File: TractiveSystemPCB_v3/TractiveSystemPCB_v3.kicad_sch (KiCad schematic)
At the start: 42 parts, among them J1 TS, Q1 2N7002, Q4 RSC002, Q7 2N7002, U1 LM311, U6 4N35, U7 NE555D

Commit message: Update KiCADReferencingInstructions.docx, TractiveSystemPCB_v3-2022-09-27_114516.zip, and 9 more files...
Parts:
- added C2: 10nF, symbol GRC_Device:C_Small
- added D?: 17VBD, symbol GRC_Device:D_Zener
- added F?: Fuse_Small, symbol GRC_Device:Fuse_Small
- added R19: 20kΩ, symbol GRC_Device:R_Small
- added R20: 1.2kΩ, symbol GRC_Device:R_Small
- added R22: 10kΩ, symbol GRC_Device:R_Small
- added R?: 0Ω, symbol GRC_Device:R_Small
- added TP4: TestPoint, symbol GRC_Connector:TestPoint
- added U5: 4N35, Package_DIP:DIP-6_W7.62mm, symbol GRC_Isolator:4N35
- gave numbers to parts that had none: 3
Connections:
- net +12V: now also U3.8 (V+), R19.2, U5.1
- net +GLV: now also U5.5
- net BusRefPrecharge: now also F?.1, R?.1
- net GLV-: now also R22.2
- net GND: now also U3.1 (GND), U3.4 (V-), D?.2 (A)
- net PrechargeRef: now reaches RV2.2, TP3.1
- net PrechargeRef: now also U3.3 (-), C2.2
- net at U3.2 (+): now also C2.1, D?.1 (K), F?.2, R?.2, TP4.1
- net at U3.5 (BAL): now also U3.6 (STRB)
- net at U3.7: now also R19.1, R20.2
- new net: R20.1, U5.2
- new net: R22.1, U5.4
- no-connect marks 1 -> 2
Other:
- note added: "Precharge Control"
- note added: "Precharge Reference"
- note added: "TSAL Reference"
- moved on the sheet: RV1, RV2, TP2, TP3, U3

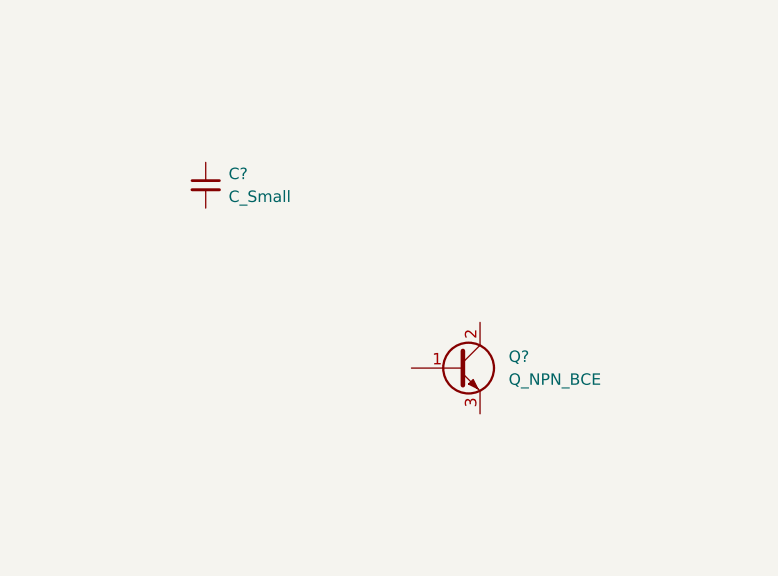
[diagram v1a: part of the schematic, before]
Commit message: Update BSPD 2.0-2022-11-05_114535.zip, Connector_Generic.kicad_sym, and 16 more files...
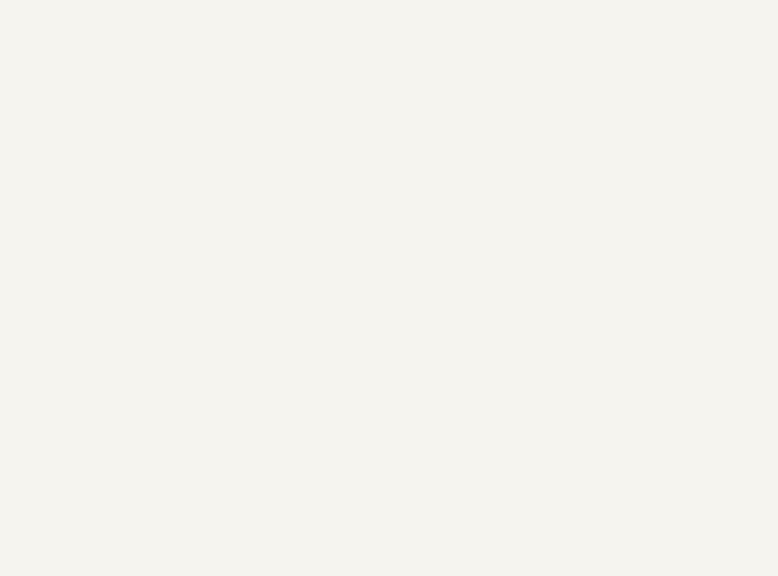
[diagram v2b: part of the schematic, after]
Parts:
- removed C?: C_Small, symbol GRC_Device:C_Small
- removed Q?: Q_NPN_BCE, symbol GRC_Device:Q_NPN_BCE
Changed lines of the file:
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@@
     (pin "1")
-  )
-  (symbol (lib_id "GRC_Device:C_Small") (at 223.52 118.11 0) (unit 1)
-    (in_bom yes) (on_board yes) (fields_autoplaced)
-    (property "Reference" "C?" (id 0) (at 226.06 116.8462 0)
-      (effects (font (size 1.27 1.27)) (justify left))
-    )
-    (property "Value" "C_Small" (id 1) (at 226.06 119.3862 0)
-      (effects (font (size 1.27 1.27)) (justify left))
-    )
-    (property "Footprint" "" (id 2) (at 223.52 118.11 0)
-      (effects (font (size 1.27 1.27)) hide)
-    )
-    (property "Datasheet" "~" (id 3) (at 223.52 118.11 0)
-      (effects (font (size 1.27 1.27)) hide)
-    )
-    (pin "1")
-    (pin "2")
   )
   (symbol (lib_id "GRC_glv-:GLV-") (at 140.335 120.015 0) (unit 1)
@@
     (pin "1")
   )
-  (symbol (lib_id "GRC_Device:Q_NPN_BCE") (at 251.46 138.43 0) (unit 1)
-    (in_bom yes) (on_board yes) (fields_autoplaced)
-    (property "Reference" "Q?" (id 0) (at 257.175 137.1599 0)
-      (effects (font (size 1.27 1.27)) (justify left))
-    )
-    (property "Value" "Q_NPN_BCE" (id 1) (at 257.175 139.6999 0)
-      (effects (font (size 1.27 1.27)) (justify left))
-    )
-    (property "Footprint" "" (id 2) (at 256.54 135.89 0)
-      (effects (font (size 1.27 1.27)) hide)
-    )
-    (property "Datasheet" "~" (id 3) (at 251.46 138.43 0)
-      (effects (font (size 1.27 1.27)) hide)
-    )
-    (pin "1")
-    (pin "2")
-    (pin "3")
-  )
   (symbol (lib_id "GRC_Device:C_Small") (at 81.915 62.865 0) (unit 1)
     (in_bom yes) (on_board yes)
@@
       (reference "C8") (unit 1) (value "100nF") (footprint "")
     )
-    (path "/22c18cbc-7d8f-4189-a06b-629302355c23"
-      (reference "C?") (unit 1) (value "C_Small") (footprint "")
-    )
     (path "/6fb6519d-1f87-4cbc-9a19-59a3ef7ce957"
       (reference "D1") (unit 1) (value "Green") (footprint "")
@@
       (reference "Q?") (unit 1) (value "RSC002") (footprint "")
     )
-    (path "/eeabaea1-8cb9-402c-a4eb-599dc7507fac"
-      (reference "Q?") (unit 1) (value "Q_NPN_BCE") (footprint "")
-    )
     (path "/fdb9292e-fadc-4f20-86c6-11d85114ee0b"
